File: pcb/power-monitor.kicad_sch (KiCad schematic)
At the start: 5 parts, among them U3 INA219BIDCNR

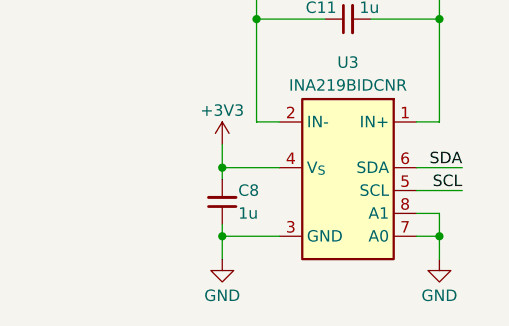
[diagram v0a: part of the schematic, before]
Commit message: [#3] Add input capacitors and power indicator LED, change GND names on primary and secondary
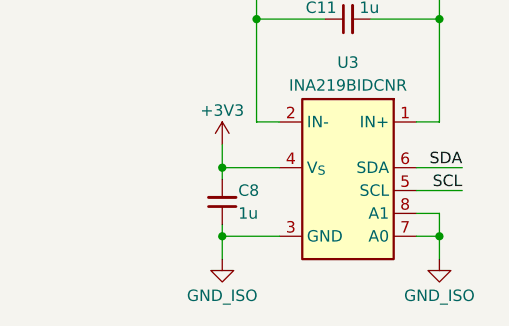
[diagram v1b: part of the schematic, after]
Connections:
- net GND renamed GND_ISO
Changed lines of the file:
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@@
+	)
+	(symbol
+		(lib_id "DW-power-symbols:GND")
+		(at 69.85 118.11 0)
+		(unit 1)
+		(exclude_from_sim no)
+		(in_bom yes)
+		(on_board yes)
+		(dnp no)
+		(property "Reference" "#PWR08"
+			(at 69.85 124.46 0)
+			(effects
+				(font
+					(size 1.27 1.27)
+				)
+				(hide yes)
+			)
+		)
+		(property "Value" "GND_ISO"
+			(at 69.85 122.174 0)
+			(effects
+				(font
+					(size 1.27 1.27)
+				)
+			)
+		)
+		(property "Footprint" ""
+			(at 69.85 118.11 0)
+			(effects
+				(font
+					(size 1.27 1.27)
+				)
+				(hide yes)
+			)
+		)
+		(property "Datasheet" ""
+			(at 69.85 118.11 0)
+			(effects
+				(font
+					(size 1.27 1.27)
+				)
+				(hide yes)
+			)
+		)
+		(property "Description" "Power symbol creates a global label with name \"GND\" , ground"
+			(at 69.85 118.11 0)
+			(effects
+				(font
+					(size 1.27 1.27)
+				)
+				(hide yes)
+			)
+		)
+		(pin "1"
+		)
+		(instances
+			(project "resonant-converter"
+				(path "/da6185c3-cd85-4a88-bee6-2ff386eae772/7e8f17cf-feda-4bf7-90f5-32e7debe11a7"
+					(reference "#PWR08")
+					(unit 1)
+				)
+			)
+		)
 	)
 	(symbol
@@
 		(lib_id "DW-power-symbols:GND")
 		(at 93.98 118.11 0)
-		(mirror y)
 		(unit 1)
 		(exclude_from_sim no)
@@
 			)
 		)
-		(property "Value" "GND"
+		(property "Value" "GND_ISO"
 			(at 93.98 122.174 0)
 			(effects
@@
 					(unit 1)
 				)
-			)
-		)
-	)
-	(symbol
-		(lib_id "DW-power-symbols:GND")
-		(at 69.85 118.11 0)
-		(mirror y)
-		(unit 1)
-		(exclude_from_sim no)
-		(in_bom yes)
-		(on_board yes)
-		(dnp no)
-		(property "Reference" "#PWR08"
-			(at 69.85 124.46 0)
-			(effects
-				(font
-					(size 1.27 1.27)
-				)
-				(hide yes)
-			)
-		)
-		(property "Value" "GND"
-			(at 69.85 122.174 0)
-			(effects
-				(font
-					(size 1.27 1.27)
-				)
-			)
-		)
-		(property "Footprint" ""
-			(at 69.85 118.11 0)
-			(effects
-				(font
-					(size 1.27 1.27)
-				)
-				(hide yes)
-			)
-		)
-		(property "Datasheet" ""
-			(at 69.85 118.11 0)
-			(effects
-				(font
-					(size 1.27 1.27)
-				)
-				(hide yes)
-			)
-		)
-		(property "Description" "Power symbol creates a global label with name \"GND\" , ground"
-			(at 69.85 118.11 0)
-			(effects
-				(font
-					(size 1.27 1.27)
-				)
-				(hide yes)
-			)
-		)
-		(pin "1"
-		)
-		(instances
-			(project "resonant-converter"
-				(path "/da6185c3-cd85-4a88-bee6-2ff386eae772/7e8f17cf-feda-4bf7-90f5-32e7debe11a7"
-					(reference "#PWR08")
-					(unit 1)
-				)

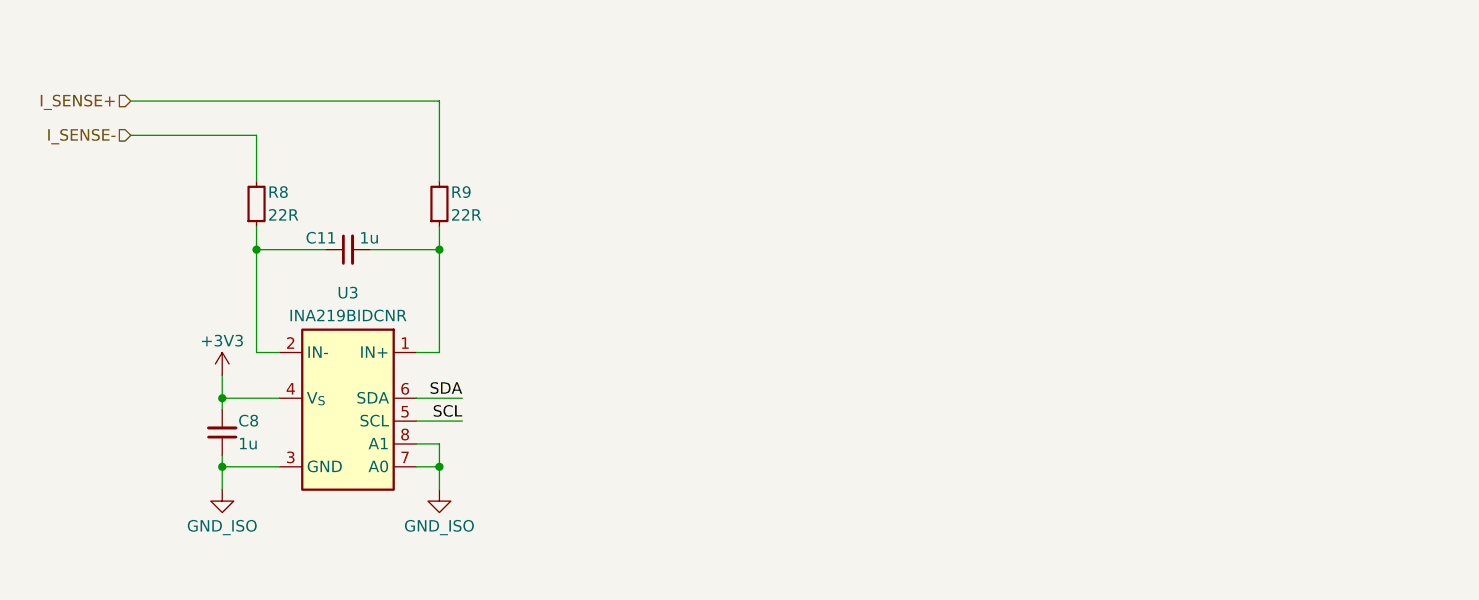
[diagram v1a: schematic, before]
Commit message: [#4] Sch: Add input and output capacitors, pri-sec interference capacitor and QWIIC connector, refactor schematic
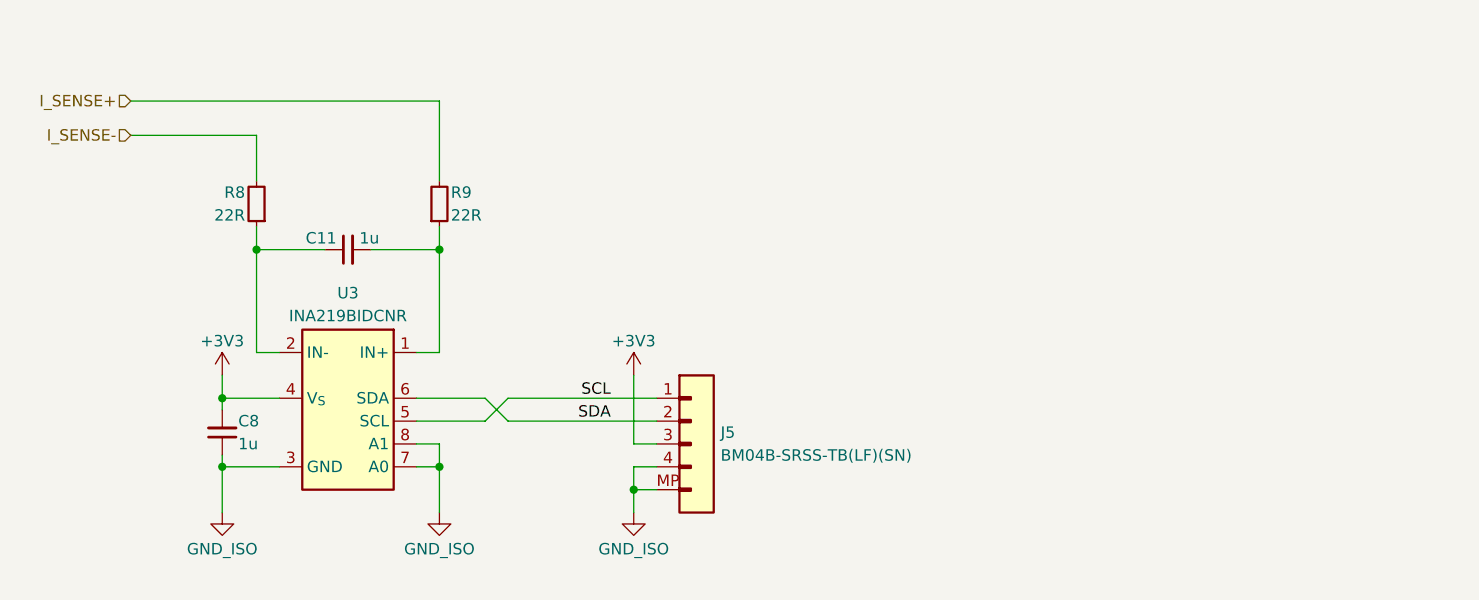
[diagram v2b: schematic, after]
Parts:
- added J5: JST_SH_1x4_BM04B-SRSS-TB-LF-SN, DW-footprints:Conn_JST_SH_1x4_BM04B-SRSS-TB, symbol DW-connectors:JST_SH_1x4_BM04B-SRSS-TB-LF-SN
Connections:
- net +3V3: now also J5.3
- net GND_ISO: now also J5.4, J5.MP
- net SCL: now also J5.1
- net SDA: now also J5.2
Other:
- moved on the sheet: R8

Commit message: [#4] Sch: Add I2C pullups, write down INA219's address, add hierarchical label for power monitor's GND
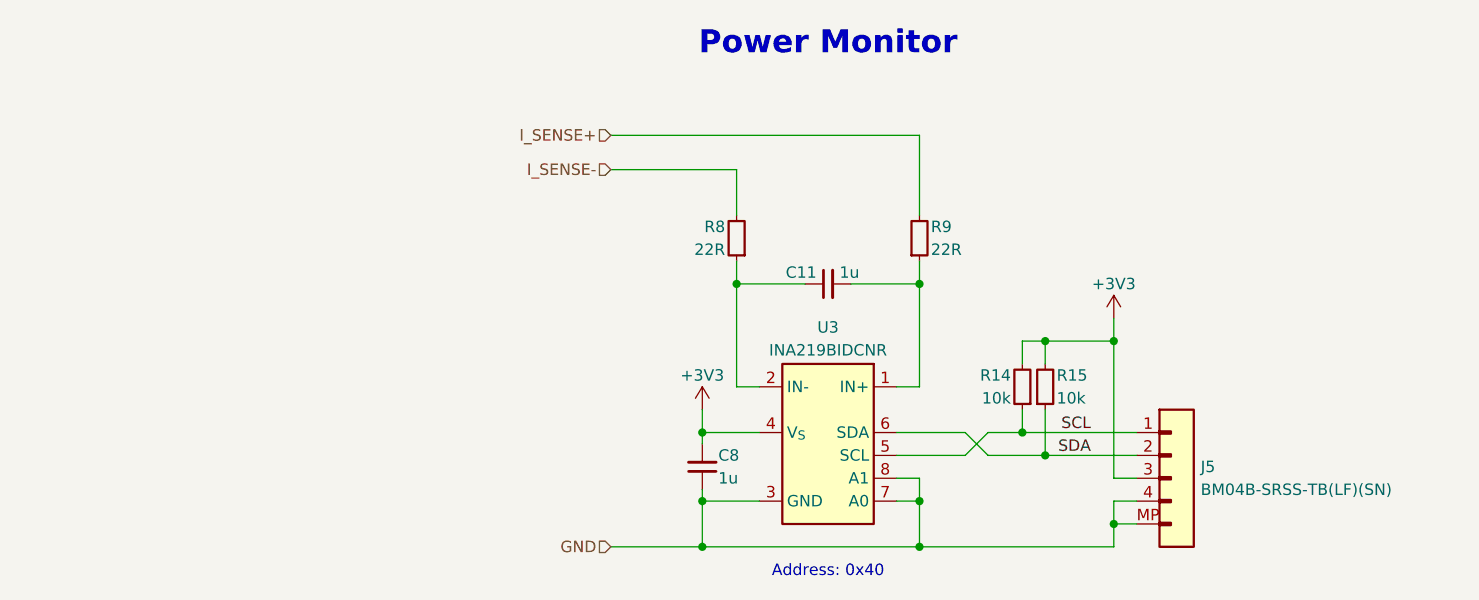
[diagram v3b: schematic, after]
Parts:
- added R14, R15: R-10k-0402, DW-footprints:R_0402_1005Metric, symbol DW-resistors:R-10k-0402
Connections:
- net +3V3: now also R14.2, R15.2
- net SCL: now also R14.1
- net SDA: now also R15.1
- net GND_ISO renamed GND
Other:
- note added: "Address: 0x40"
- note added: "Power Monitor"
- moved on the sheet: C11, C8, J5, R8, R9, U3

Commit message: [#4] Sch: Fill out title block in power monitor sheet
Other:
- title: (none) -> Resonant Converter
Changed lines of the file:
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@@
 	(generator_version "9.0")
 	(paper "A4")
+	(title_block
+		(title "Resonant Converter")
+		(date "2026-03-24")
+		(rev "1.0.0")
+		(comment 1 "Project authors: Maksim Kondratovich, Dominik Pluta")
+	)
 	(text "Address: 0x40"
 		(exclude_from_sim no)

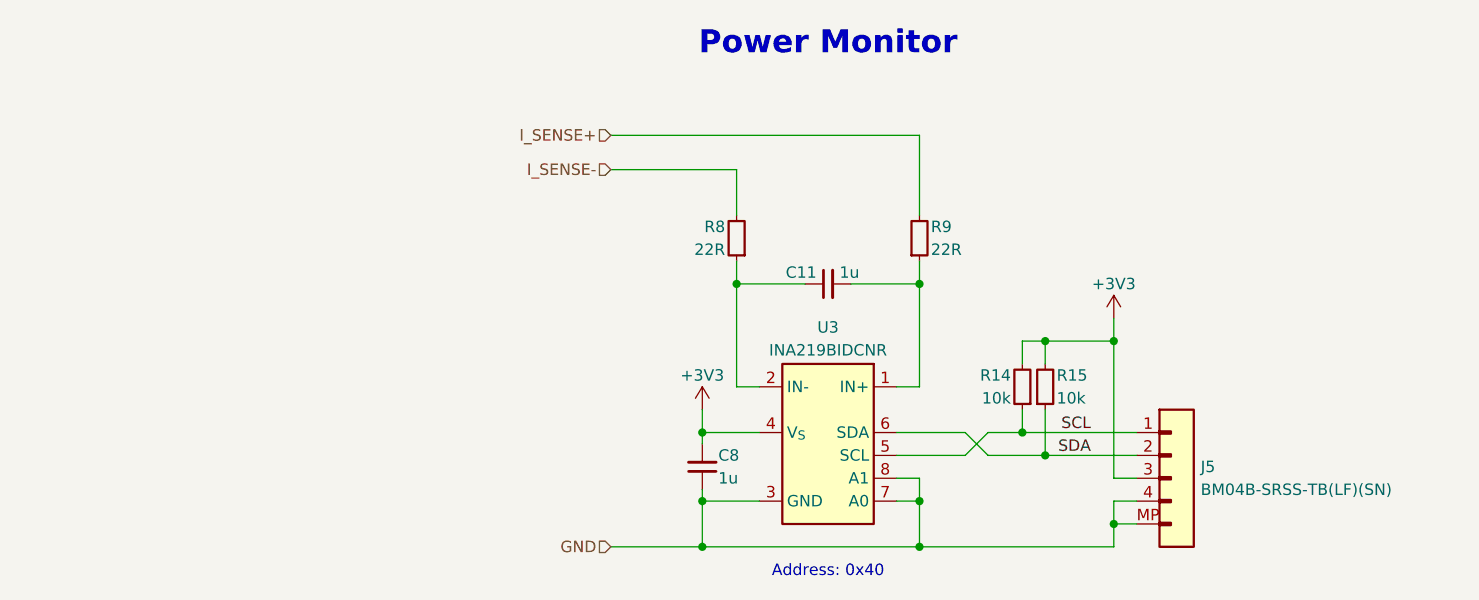
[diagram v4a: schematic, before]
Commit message: Re-annotate schematic, update PCB from schematic
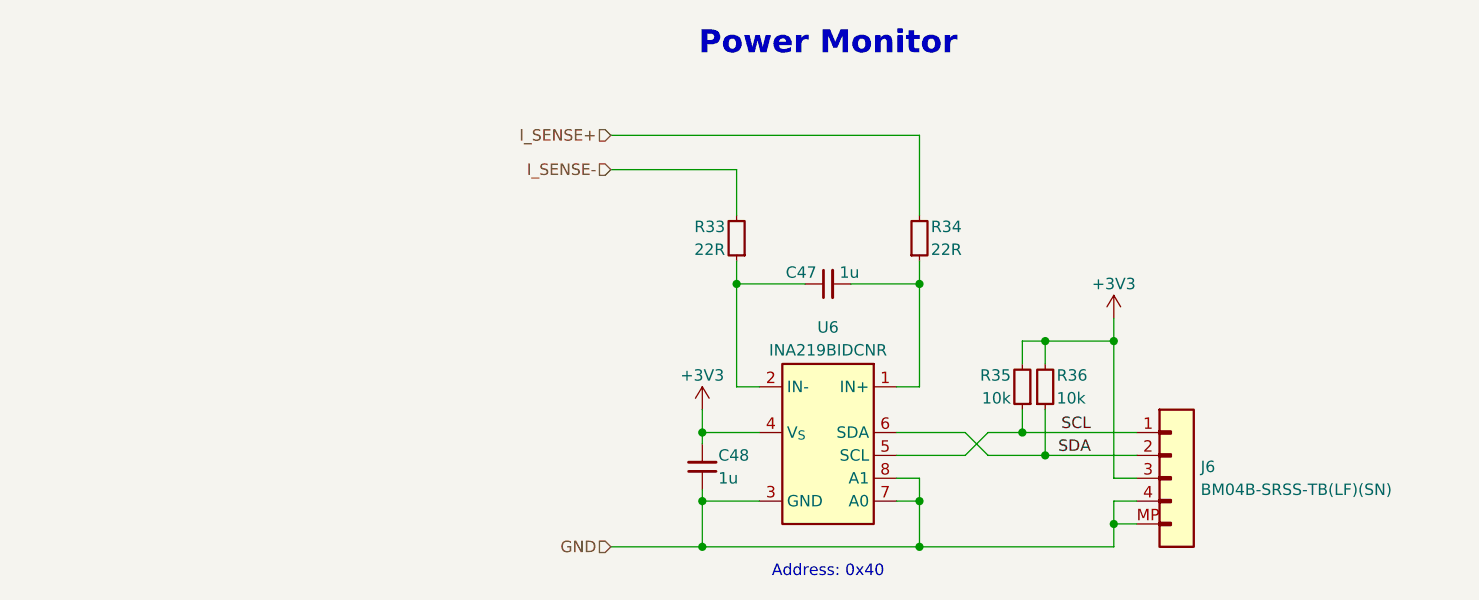
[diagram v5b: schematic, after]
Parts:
- renumbered C11 to C47, C8 to C48, J5 to J6, R8 to R33, R9 to R34, R14 to R35, R15 to R36, U3 to U6
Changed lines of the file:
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@@
 		(on_board yes)
 		(dnp no)
-		(property "Reference" "#PWR012"
+		(property "Reference" "#PWR027"
 			(at 168.91 102.87 0)
 			(effects
@@
 			(project "resonant-converter"
 				(path "/da6185c3-cd85-4a88-bee6-2ff386eae772/7e8f17cf-feda-4bf7-90f5-32e7debe11a7"
-					(reference "#PWR012")
+					(reference "#PWR027")
 					(unit 1)
 				)
@@
 		(on_board yes)
 		(dnp no)
-		(property "Reference" "C8"
+		(property "Reference" "C48"
 			(at 124.968 114.3 90)
 			(effects
@@
 			(project "resonant-converter"
 				(path "/da6185c3-cd85-4a88-bee6-2ff386eae772/7e8f17cf-feda-4bf7-90f5-32e7debe11a7"
-					(reference "C8")
+					(reference "C48")
 					(unit 1)
 				)
@@
 		(on_board yes)
 		(dnp no)
-		(property "Reference" "J5"
+		(property "Reference" "J6"
 			(at 178.562 115.57 0)
 			(effects
@@
 			(project "resonant-converter"
 				(path "/da6185c3-cd85-4a88-bee6-2ff386eae772/7e8f17cf-feda-4bf7-90f5-32e7debe11a7"
-					(reference "J5")
+					(reference "J6")
 					(unit 1)
 				)
@@
 		(on_board yes)
 		(dnp no)
-		(property "Reference" "R14"
+		(property "Reference" "R35"
 			(at 157.48 105.41 90)
 			(effects
@@
 			(project "resonant-converter"
 				(path "/da6185c3-cd85-4a88-bee6-2ff386eae772/7e8f17cf-feda-4bf7-90f5-32e7debe11a7"
-					(reference "R14")
+					(reference "R35")
 					(unit 1)
 				)
@@
 		(on_board yes)
 		(dnp no)
-		(property "Reference" "R8"
+		(property "Reference" "R33"
 			(at 125.73 88.9 90)
 			(effects
@@
 			(project "resonant-converter"
 				(path "/da6185c3-cd85-4a88-bee6-2ff386eae772/7e8f17cf-feda-4bf7-90f5-32e7debe11a7"
-					(reference "R8")
+					(reference "R33")
 					(unit 1)
 				)
@@
 		(on_board yes)
 		(dnp no)
-		(property "Reference" "#PWR010"
+		(property "Reference" "#PWR028"
 			(at 123.19 113.03 0)
 			(effects
@@
 			(project "resonant-converter"
 				(path "/da6185c3-cd85-4a88-bee6-2ff386eae772/7e8f17cf-feda-4bf7-90f5-32e7debe11a7"
-					(reference "#PWR010")
+					(reference "#PWR028")
 					(unit 1)
 				)
@@
 		(on_board yes)
 		(dnp no)
-		(property "Reference" "R9"
+		(property "Reference" "R34"
 			(at 148.59 88.9 90)
 			(effects
@@
 			(project "resonant-converter"
 				(path "/da6185c3-cd85-4a88-bee6-2ff386eae772/7e8f17cf-feda-4bf7-90f5-32e7debe11a7"
-					(reference "R9")
+					(reference "R34")
 					(unit 1)
 				)
@@
 		(on_board yes)
 		(dnp no)
-		(property "Reference" "R15"
+		(property "Reference" "R36"
 			(at 162.56 105.41 90)
 			(effects
@@
 			(project "resonant-converter"
 				(path "/da6185c3-cd85-4a88-bee6-2ff386eae772/7e8f17cf-feda-4bf7-90f5-32e7debe11a7"
-					(reference "R15")
+					(reference "R36")
 					(unit 1)
 				)
@@
 		(on_board yes)
 		(dnp no)
-		(property "Reference" "U3"
+		(property "Reference" "U6"
 			(at 137.16 100.076 0)
 			(effects
@@
 			(project "resonant-converter"
 				(path "/da6185c3-cd85-4a88-bee6-2ff386eae772/7e8f17cf-feda-4bf7-90f5-32e7debe11a7"
-					(reference "U3")
+					(reference "U6")
 					(unit 1)
 				)
@@
 		(on_board yes)
 		(dnp no)
-		(property "Reference" "C11"
+		(property "Reference" "C47"
 			(at 135.89 93.98 0)
 			(effects
@@
 			(project ""
 				(path "/da6185c3-cd85-4a88-bee6-2ff386eae772/7e8f17cf-feda-4bf7-90f5-32e7debe11a7"
-					(reference "C11")
+					(reference "C47")
 					(unit 1)
 				)

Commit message: Sch: Add test points and 3V3 power indicator LED
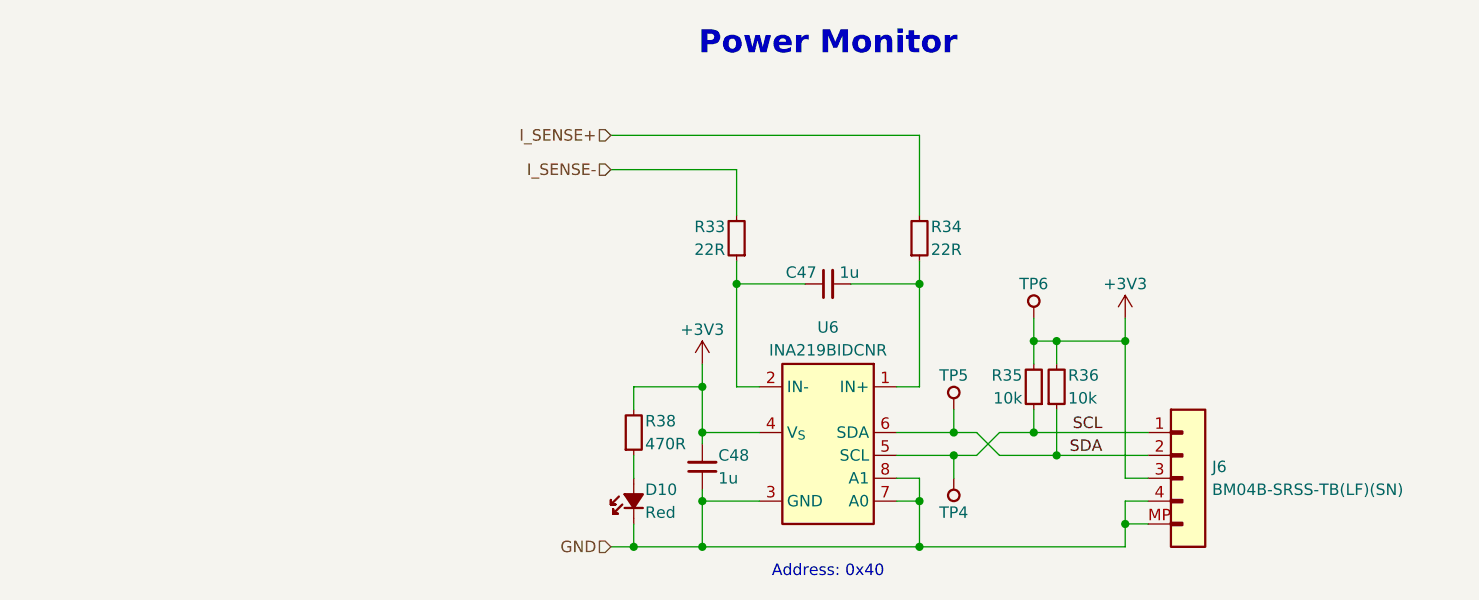
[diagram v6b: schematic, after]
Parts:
- added D10: LED-R-0603_KT-0603R, DW-footprints:LED_0603_1608Metric_R, symbol DW-diodes:LED-R-0603_KT-0603R
- added R38: R-470R-0402, DW-footprints:R_0402_1005Metric, symbol DW-resistors:R-470R-0402
- added TP4, TP5, TP6: TP_SMD_1mm, DW-footprints:TP_SMD_1mm, symbol DW-test-points:TP_SMD_1mm
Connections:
- net +3V3: now also R38.2, TP6.1
- net GND: now also D10.1 (C)
- net SCL: now also TP4.1
- net SDA: now also TP5.1
- new net: D10.2 (A), R38.1
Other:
- moved on the sheet: J6, R35, R36

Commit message: Sch: Re-annotate schematic, clear ERC
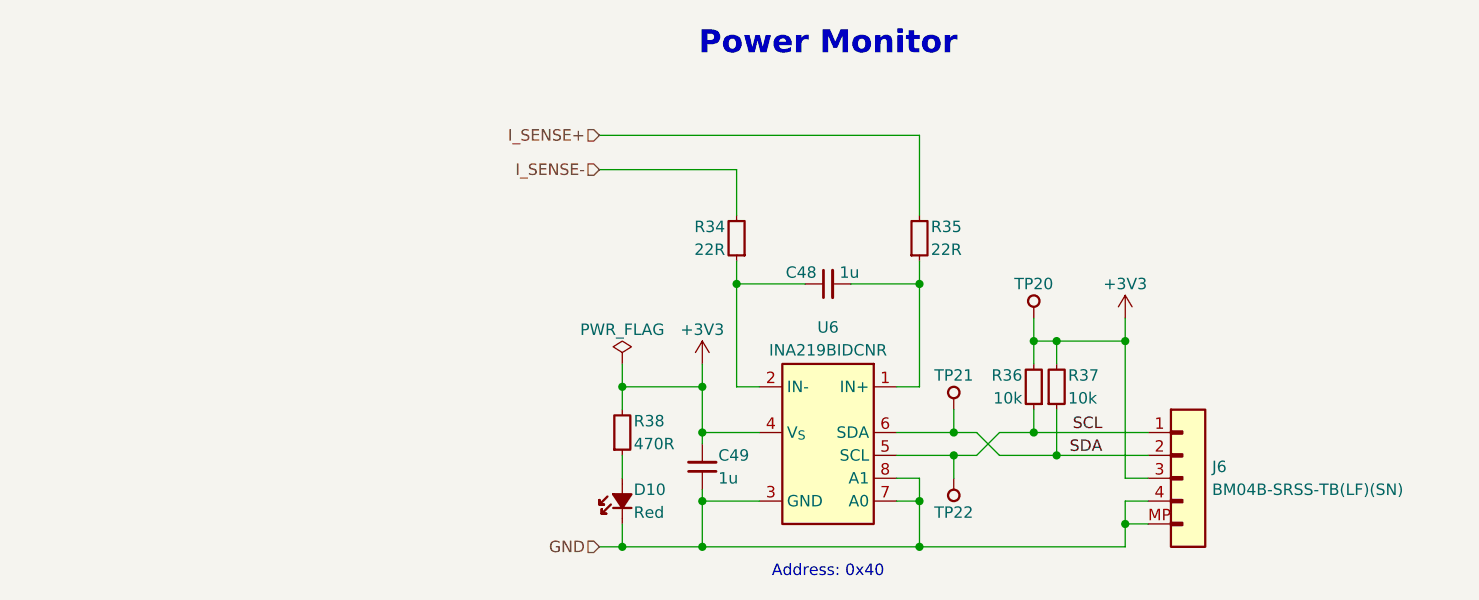
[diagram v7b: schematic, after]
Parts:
- renumbered C47 to C48, C48 to C49, R33 to R34, R34 to R35, R35 to R36, R36 to R37, TP6 to TP20, TP5 to TP21, TP4 to TP22
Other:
- moved on the sheet: D10, R38
